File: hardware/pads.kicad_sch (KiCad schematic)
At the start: 56 parts, among them J1 5V, J10 5V, J11 5V, J12 5V, J13 5V, J14 5V, J15 5V, J16 5V, J17 5V, J18 5V, J19 5V, J2 5V, J20 5V, J21 5V, J22 5V, J23 5V, J24 5V, J25 5V, J26 5V, J27 5V, J28 5V, J29 5V, J3 5V, J30 5V, J31 5V, J32 5V, J33 5V, J34 5V, J35 5V, J36 5V, J37 5V, J38 5V, J39 5V, J4 5V, J40 5V, J41 5V, J42 5V, J43 5V, J44 5V, J45 5V, J46 5V, J47 5V, J48 5V, J49 5V, J5 5V, J50 5V, J51 5V, J52 5V, J53 5V, J54 5V, J6 5V, J7 5V, J8 5V, J9 5V, P1 SM08B-SRSS-TB(LF)(SN), U8 SM06B-SRSS-TB(LF)(SN)

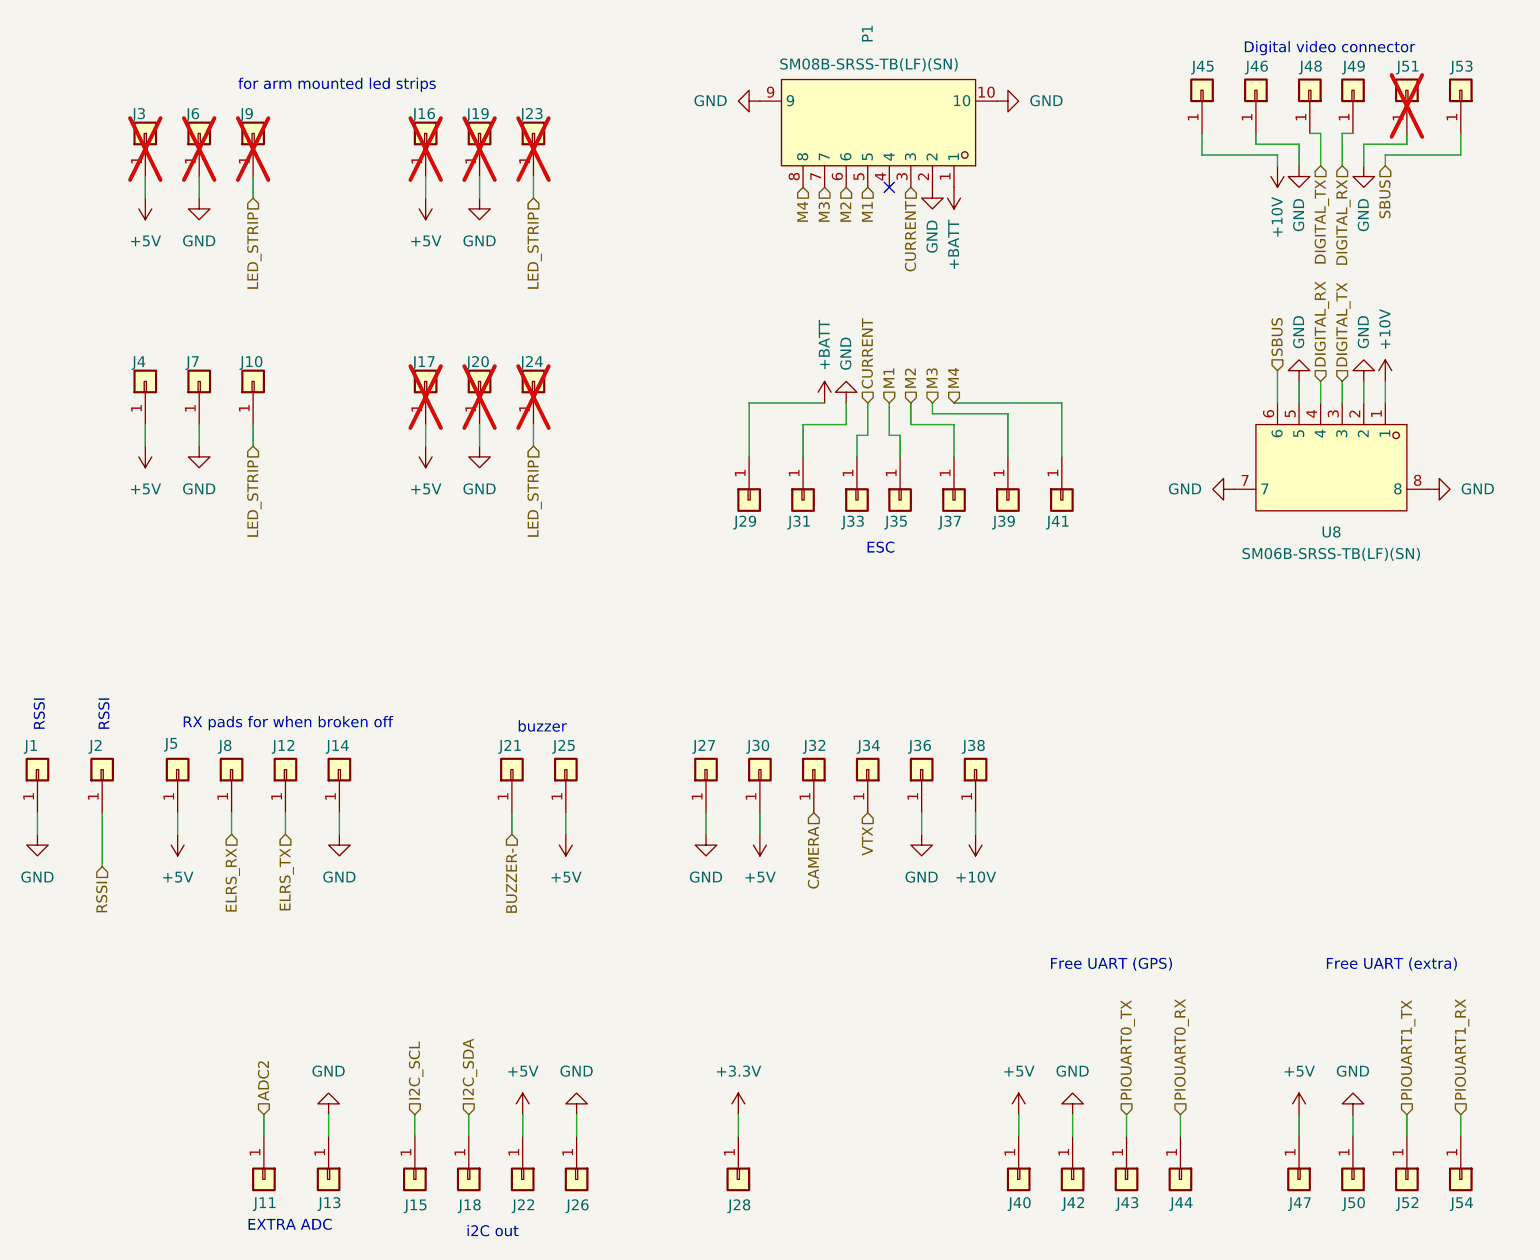
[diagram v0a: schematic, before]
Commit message: many tiny improvements
- I/O correctness
- SPI0/SPI1/I2C0 bus corrections
- decoupling of DVDD
- ADC_AVDD as per RPi documents
- removal of SBUS
- connect ESC serial
- remove RUN RC-circuit as per RPi documentation
- some more cleanup for readability
- gyro CLKIN decision
- I2C 4.7k pullup
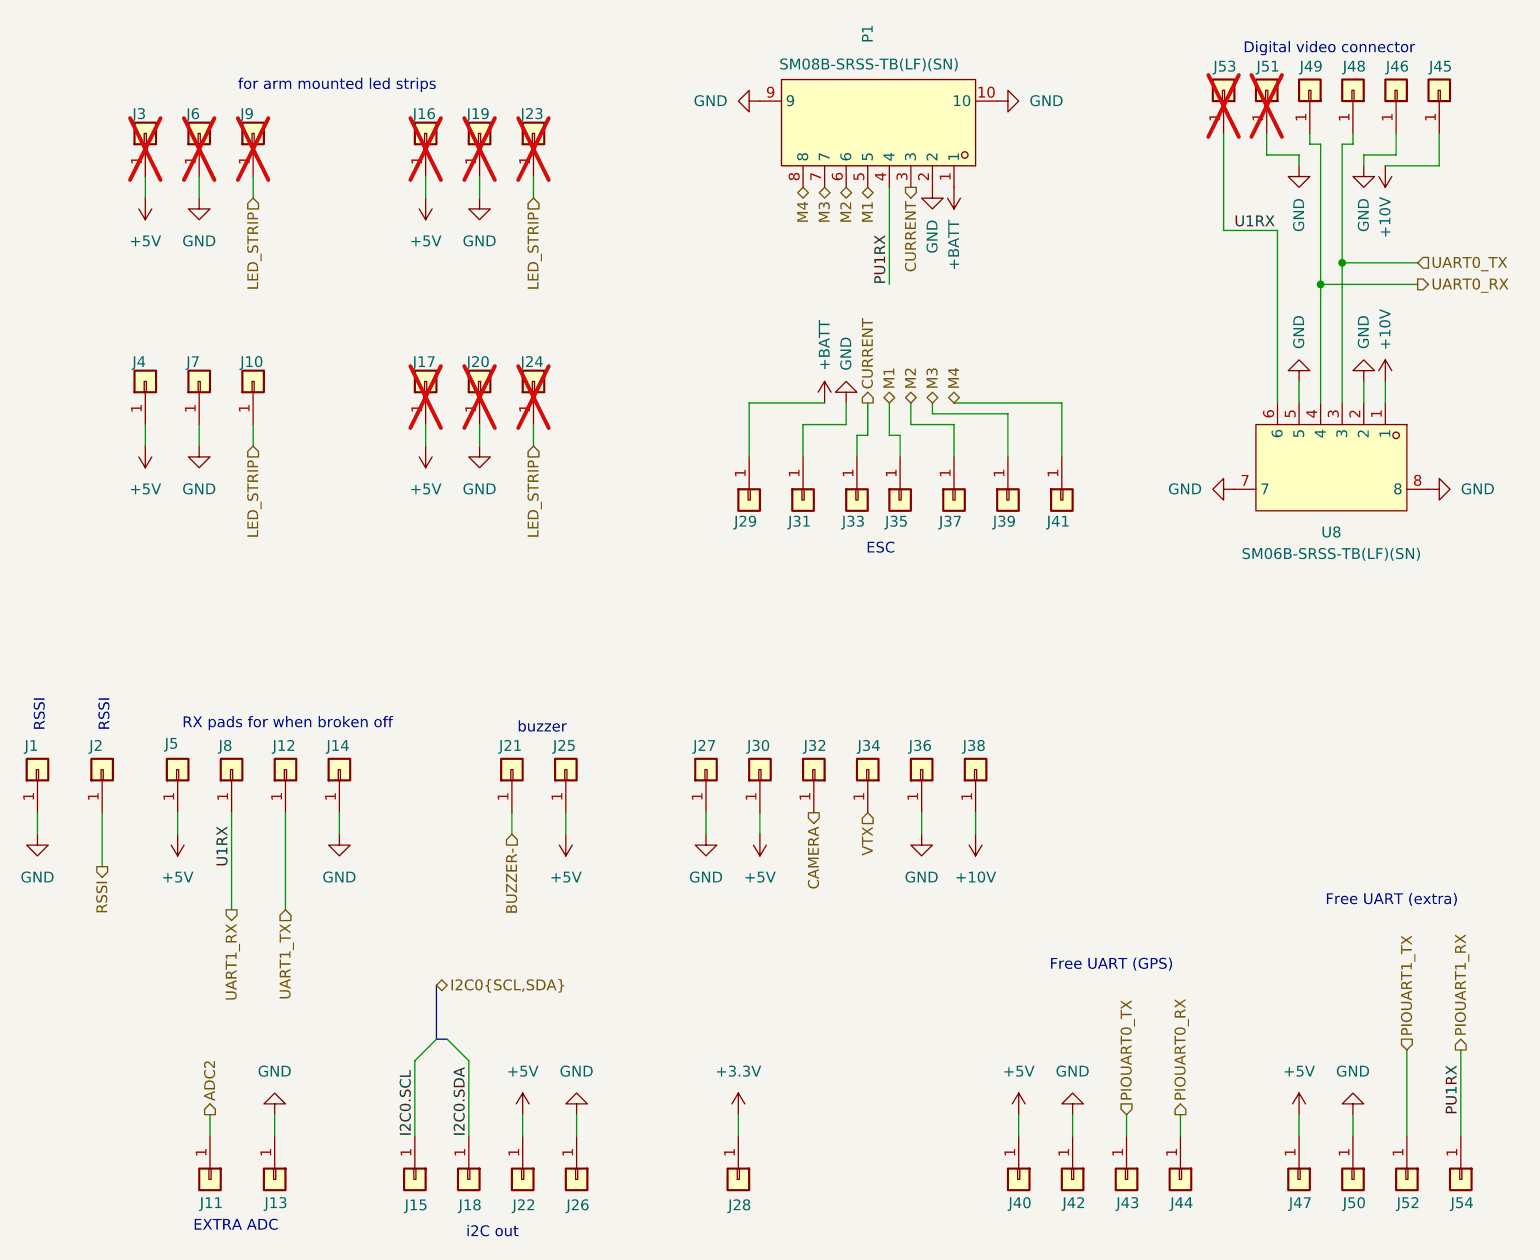
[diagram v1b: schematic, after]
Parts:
- J53: now not fitted
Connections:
- net SBUS is gone; now on net UART1_RX: J53.1 (Pin_1), U8.6
- net PIOUART1_RX: now also P1.4
- net DIGITAL_RX renamed UART0_RX
- net DIGITAL_TX renamed UART0_TX
- net ELRS_RX renamed UART1_RX
- net ELRS_TX renamed UART1_TX
- net I2C_SCL renamed I2C0.SCL
- net I2C_SDA renamed I2C0.SDA
- no-connect marks 1 -> 0
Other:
- moved on the sheet: J11, J13, J45, J46, J48, J49, J51

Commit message: RP2354A
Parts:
- J1, J11, J13, J2, J36, J38, J47, J50, J52, J54: now not fitted
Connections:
- net PIOUART0_RX: now also J53.1 (Pin_1), J8.1 (Pin_1), U8.6; no longer J44.1 (Pin_1)
- net PIOUART0_TX: now also J12.1 (Pin_1); no longer J43.1 (Pin_1)
- net UART1_RX: now also J44.1 (Pin_1); no longer J53.1 (Pin_1), J8.1 (Pin_1), U8.6
- net UART1_TX: now also J43.1 (Pin_1); no longer J12.1 (Pin_1)
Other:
- note added: "Camera + VTX"
- note added: "RX pads"
- note removed: "RX pads for when broken off"
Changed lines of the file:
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@@
 		)
 	)
-	(text "RX pads for when broken off"
+	(text "RX pads"
 		(exclude_from_sim no)
-		(at 62.484 97.536 0)
+		(at 59.436 96.774 0)
 		(effects
 			(font
@@
 		)
 	)
+	(text "Camera + VTX"
+		(exclude_from_sim no)
+		(at 128.27 97.028 0)
+		(effects
+			(font
+				(size 1.27 1.27)
+			)
+		)
+	)
 	(text "Digital video connector"
 		(exclude_from_sim no)
@@
 	)
 	(bus_entry
-		(at 80.01 134.62)
+		(at 81.28 134.62)
 		(size -2.54 2.54)
 		(stroke
@@
 	(wire
 		(pts
+			(xy 78.74 138.43) (xy 77.47 138.43)
+		)
+		(stroke
+			(width 0)
+			(type default)
+		)
+	)
+	(wire
+		(pts
 			(xy 111.76 107.95) (xy 111.76 110.49)
 		)
@@
 	(wire
 		(pts
+			(xy 77.47 138.43) (xy 77.47 146.05)
+		)
+		(stroke
+			(width 0)
+			(type default)
+		)
+	)
+	(wire
+		(pts
 			(xy 52.07 33.02) (xy 52.07 35.56)
 		)
@@
 	(wire
 		(pts
-			(xy 77.47 137.16) (xy 77.47 146.05)
+			(xy 78.74 137.16) (xy 78.74 138.43)
 		)
 		(stroke
@@
 	(wire
 		(pts
+			(xy 55.88 107.95) (xy 55.88 115.57)
+		)
+		(stroke
+			(width 0)
+			(type default)
+		)
+	)
+	(wire
+		(pts
 			(xy 115.57 146.05) (xy 115.57 143.51)
 		)
@@
 	(wire
 		(pts
-			(xy 62.23 107.95) (xy 62.23 119.38)
+			(xy 62.23 107.95) (xy 62.23 115.57)
 		)
 		(stroke
@@
 	(bus
 		(pts
-			(xy 80.01 128.27) (xy 80.01 134.62)
+			(xy 81.28 128.27) (xy 81.28 134.62)
 		)
 		(stroke
@@
 	(wire
 		(pts
-			(xy 55.88 107.95) (xy 55.88 119.38)
-		)
-		(stroke
-			(width 0)
-			(type default)
-		)
-	)
-	(wire
-		(pts
 			(xy 187.96 146.05) (xy 187.96 143.51)
 		)
@@
 		)
 	)
-	(bus
-		(pts
-			(xy 80.01 134.62) (xy 81.28 134.62)
-		)
-		(stroke
-			(width 0)
-			(type default)
+	(label "UP0RX"
+		(at 172.72 39.37 180)
+		(effects
+			(font
+				(size 1.27 1.27)
+			)
+			(justify right bottom)
 		)
 	)
-	(label "U1RX"
+	(label "UP0RX"
 		(at 55.88 114.3 90)
 		(effects
@@
 		)
 	)
-	(label "U1RX"
-		(at 173.99 39.37 0)
-		(effects
-			(font
-				(size 1.27 1.27)
-			)
-			(justify left bottom)
-		)
-	)
 	(label "PU1RX"
 		(at 200.66 143.51 90)
@@
 		)
 	)
-	(hierarchical_label "PIOUART0_RX"
-		(shape output)
-		(at 167.64 143.51 90)
-		(effects
-			(font
-				(size 1.27 1.27)
-			)
-			(justify left)
-		)
-	)
 	(hierarchical_label "CAMERA"
 		(shape output)
@@
 	(hierarchical_label "PIOUART0_TX"
 		(shape input)
-		(at 161.29 143.51 90)
+		(at 62.23 115.57 270)
 		(effects
 			(font
 				(size 1.27 1.27)
 			)
-			(justify left)
+			(justify right)
 		)
 	)
@@
 	(hierarchical_label "I2C0{SCL,SDA}"
 		(shape bidirectional)
-		(at 80.01 128.27 0)
+		(at 81.28 128.27 0)
 		(effects
 			(font
@@
 		)
 	)
+	(hierarchical_label "PIOUART0_RX"
+		(shape output)
+		(at 55.88 115.57 270)
+		(effects
+			(font
+				(size 1.27 1.27)
+			)
+			(justify right)
+		)
+	)
 	(hierarchical_label "M1"
 		(shape bidirectional)
@@
 		)
 	)
-	(hierarchical_label "CURRENT"
+	(hierarchical_label "UART1_RX"
 		(shape output)
-		(at 130.81 59.69 90)
+		(at 167.64 143.51 90)
 		(effects
 			(font
@@
 		)
 	)
-	(hierarchical_label "RSSI"
+	(hierarchical_label "CURRENT"
 		(shape output)
-		(at 40.64 114.3 270)
+		(at 130.81 59.69 90)
 		(effects
 			(font
 				(size 1.27 1.27)
 			)
-			(justify right)
+			(justify left)
 		)
 	)
-	(hierarchical_label "UART1_RX"
+	(hierarchical_label "RSSI"
 		(shape output)
-		(at 55.88 119.38 270)
+		(at 40.64 114.3 270)
 		(effects
 			(font
@@
 		)
 	)
-	(hierarchical_label "UART1_TX"
-		(shape input)
-		(at 62.23 119.38 270)
-		(effects
-			(font
-				(size 1.27 1.27)
-			)
-			(justify right)
-		)
-	)
 	(hierarchical_label "PIOUART1_RX"
 		(shape output)
@@
 		)
 	)
+	(hierarchical_label "UART1_TX"
+		(shape input)
+		(at 161.29 143.51 90)
+		(effects
+			(font
+				(size 1.27 1.27)
+			)
+			(justify left)
+		)
+	)
 	(hierarchical_label "VTX"
 		(shape input)
@@
 		(exclude_from_sim no)
 		(in_bom no)
-		(on_board yes)
+		(on_board no)
 		(in_pos_files yes)
-		(dnp no)
+		(dnp yes)
 		(property "Reference" "J50"
 			(at 189.484 153.924 90)
@@
 		(exclude_from_sim no)
 		(in_bom no)
-		(on_board yes)
+		(on_board no)
 		(in_pos_files yes)
-		(dnp no)
+		(dnp yes)
 		(fields_autoplaced yes)
 		(property "Reference" "#PWR087"
@@
 		(exclude_from_sim no)
 		(in_bom no)
-		(on_board yes)
+		(on_board no)
 		(in_pos_files yes)
-		(dnp no)
+		(dnp yes)
 		(property "Reference" "J36"
 			(at 135.636 100.076 90)
@@
 		(exclude_from_sim no)
 		(in_bom no)
-		(on_board yes)
+		(on_board no)
 		(in_pos_files yes)
-		(dnp no)
+		(dnp yes)
 		(property "Reference" "J38"
 			(at 141.986 100.076 90)
@@
 		(exclude_from_sim no)
 		(in_bom no)
-		(on_board yes)
+		(on_board no)
 		(in_pos_files yes)
-		(dnp no)
+		(dnp yes)
 		(property "Reference" "J1"
 			(at 31.496 100.076 90)
@@
 		(exclude_from_sim no)
 		(in_bom no)
-		(on_board yes)
+		(on_board no)
 		(in_pos_files yes)
-		(dnp no)
+		(dnp yes)
 		(property "Reference" "J13"
 			(at 62.484 153.924 90)
@@
 		(exclude_from_sim no)
 		(in_bom no)
-		(on_board yes)
+		(on_board no)
 		(in_pos_files yes)
-		(dnp no)
+		(dnp yes)
 		(property "Reference" "J2"
 			(at 39.116 100.076 90)
@@
 		(exclude_from_sim no)
 		(in_bom no)
-		(on_board yes)
+		(on_board no)
 		(in_pos_files yes)
-		(dnp no)
+		(dnp yes)
 		(property "Reference" "J54"
 			(at 202.184 153.924 90)
@@
 		(exclude_from_sim no)
 		(in_bom no)
-		(on_board yes)
+		(on_board no)
 		(in_pos_files yes)
-		(dnp no)
+		(dnp yes)
 		(property "Reference" "J11"
 			(at 54.864 153.924 90)
@@
 		(exclude_from_sim no)
 		(in_bom no)
-		(on_board yes)
+		(on_board no)
 		(in_pos_files yes)
-		(dnp no)
+		(dnp yes)
 		(property "Reference" "J47"
 			(at 183.134 153.924 90)
@@
 		(exclude_from_sim no)
 		(in_bom no)
-		(on_board yes)
+		(on_board no)
 		(in_pos_files yes)
-		(dnp no)
+		(dnp yes)
 		(property "Reference" "J52"
 			(at 195.834 153.924 90)
